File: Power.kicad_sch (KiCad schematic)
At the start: 23 parts, among them U1 21700_DUAL_HOLDER, U2 TPS63070RNMR, U3 TPRT9013-33

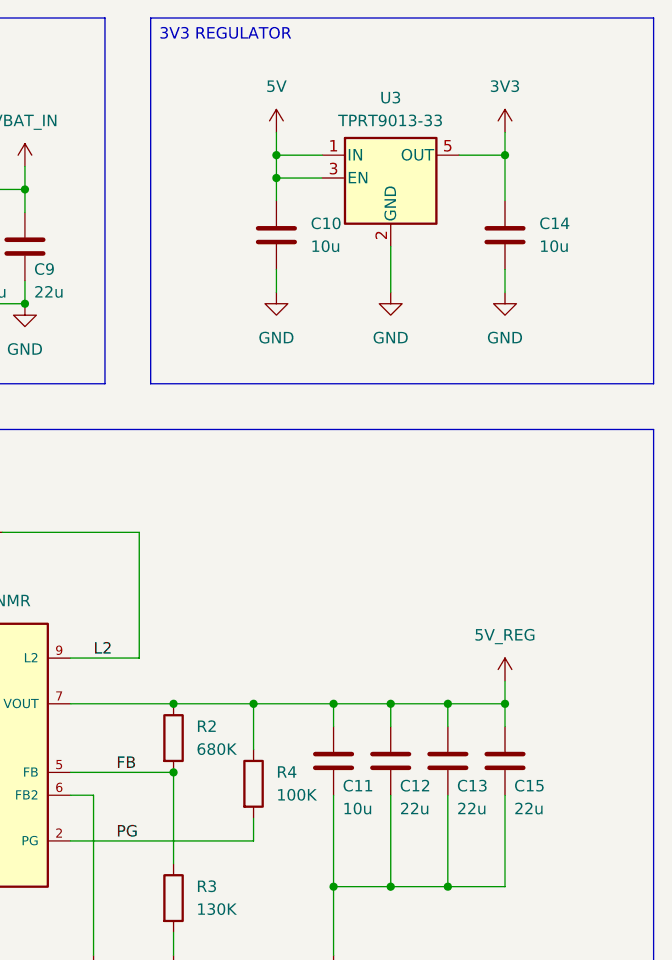
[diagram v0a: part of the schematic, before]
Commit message: Net nodes
Added the missing net nodes in the schematic.
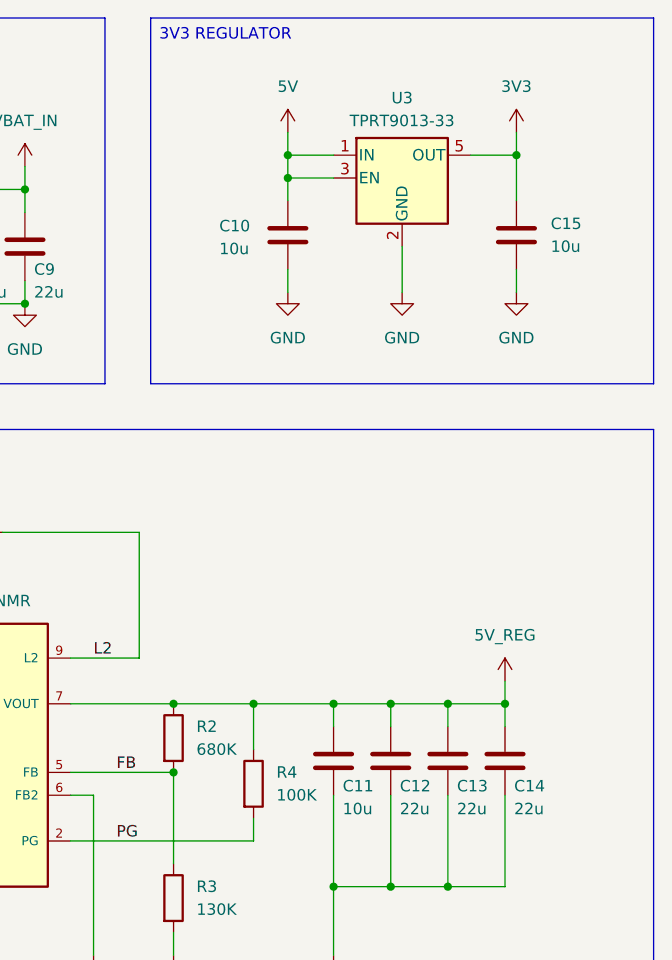
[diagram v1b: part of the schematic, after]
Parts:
- renumbered C15 to C14, C14 to C15
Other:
- moved on the sheet: C10, C15, U3

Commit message: ESC layout and footprints
Added the initial ESC layout.
Updated some footprints for compatibility.
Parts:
- C11, C3: footprint Capacitor_SMD:C_0805_2012Metric -> Capacitor_SMD:C_0603_1608Metric
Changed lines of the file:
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@@
 			)
 		)
-		(property "Footprint" "Capacitor_SMD:C_0805_2012Metric"
+		(property "Footprint" "Capacitor_SMD:C_0603_1608Metric"
 			(at 176.2252 120.65 0)
 			(effects
@@
 			)
 		)
-		(property "Footprint" "Capacitor_SMD:C_0805_2012Metric"
+		(property "Footprint" "Capacitor_SMD:C_0603_1608Metric"
 			(at 98.0948 120.65 0)
 			(effects

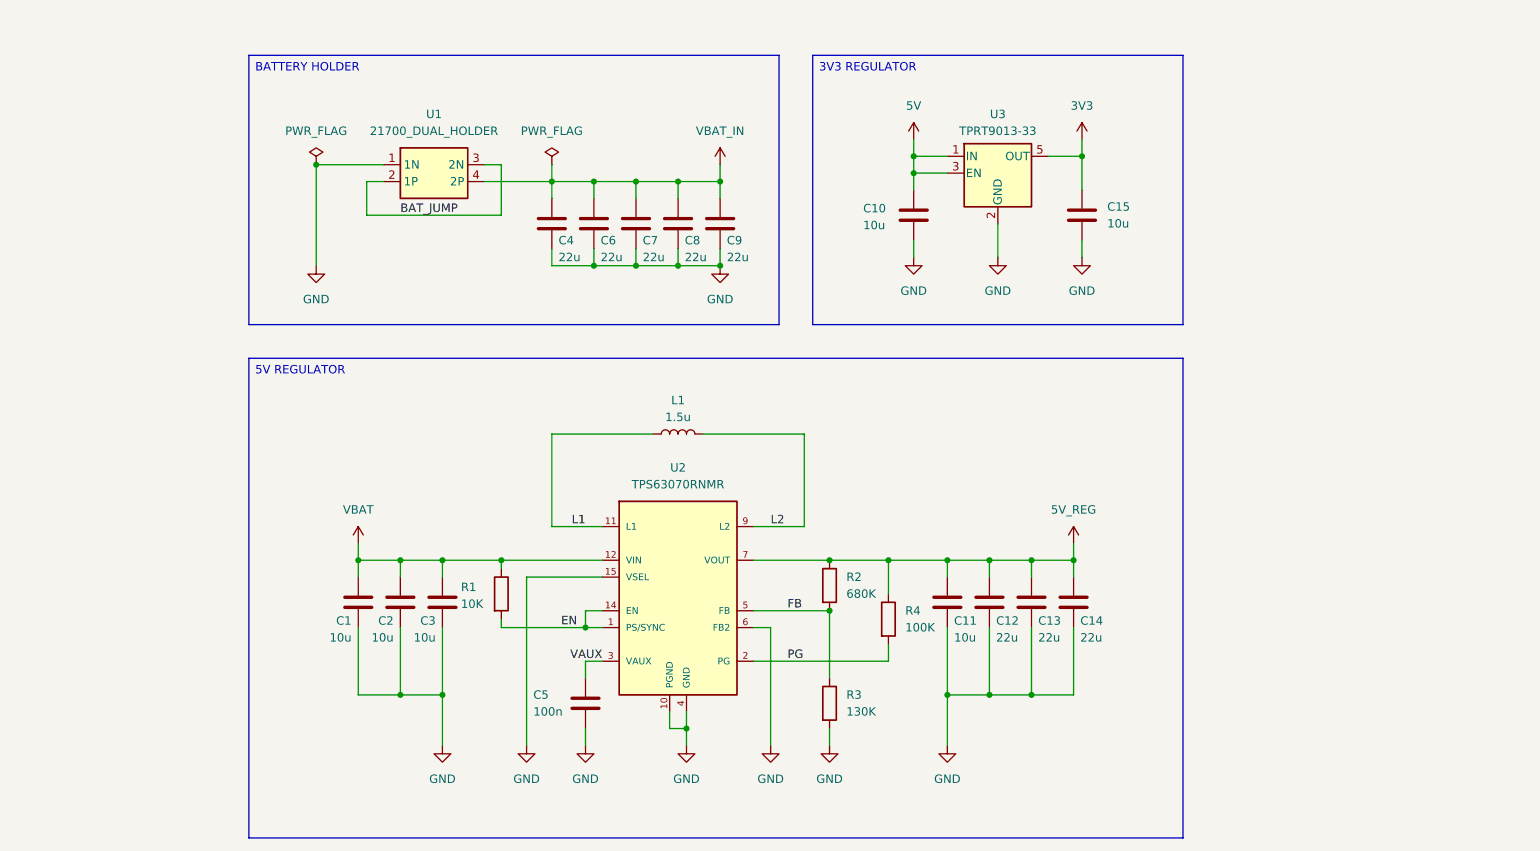
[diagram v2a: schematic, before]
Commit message: Initial layout
Completed an initial layout of the main components.

TODO
Route the ESCs and check the result.
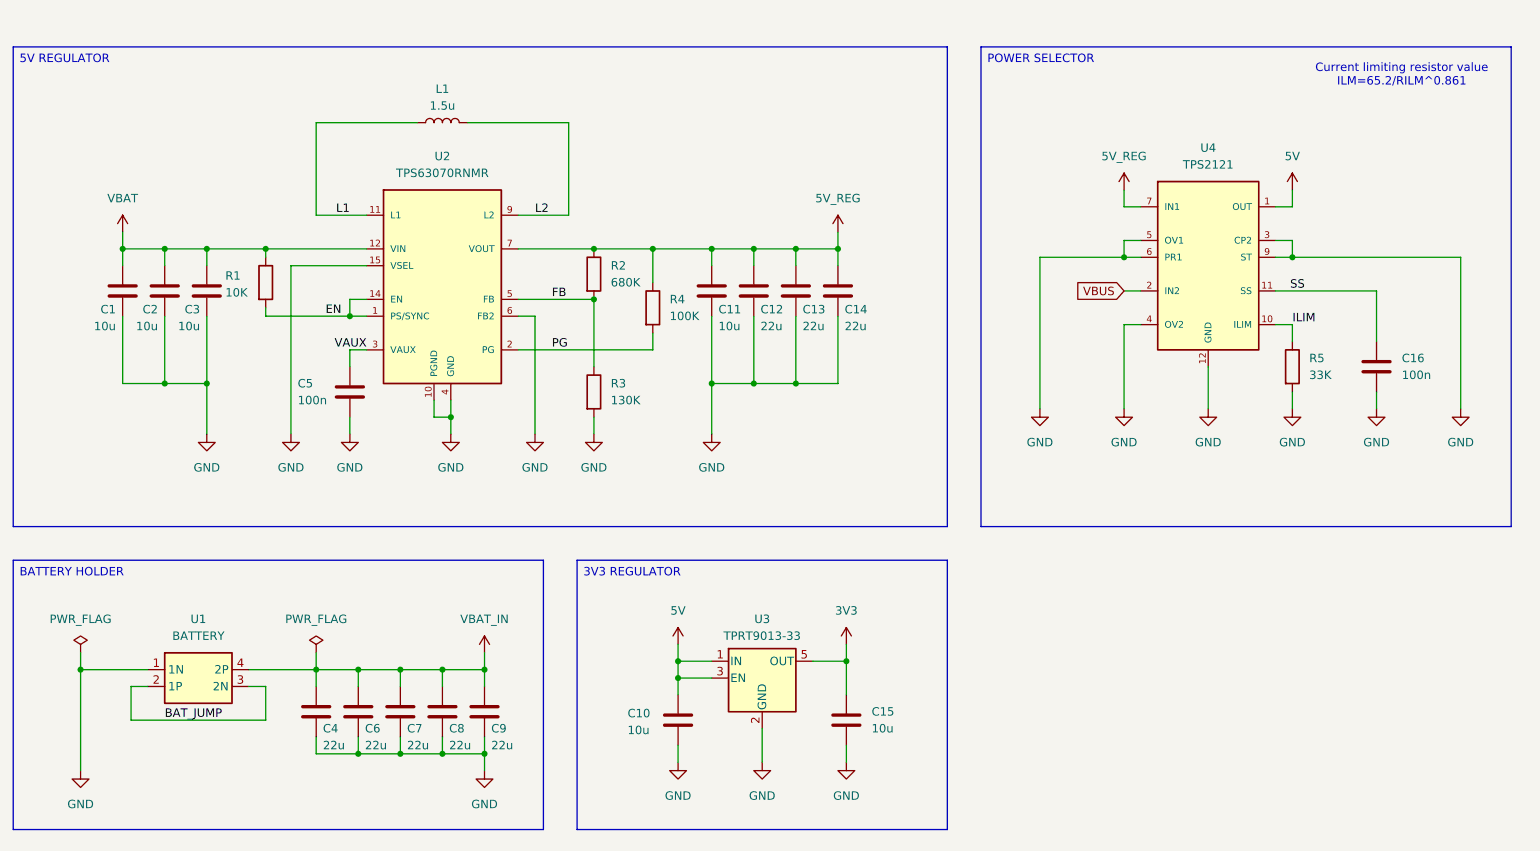
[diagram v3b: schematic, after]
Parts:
- added C16: 100n, Capacitor_SMD:C_0603_1608Metric, symbol Device:C
- added R5: 33K, Resistor_SMD:R_0603_1608Metric, symbol Device:R
- added U4: TPS2121, Custom_Parts:VQFN-HR-12_2x2.5mm_P0.5mm, symbol Custom_Parts:TPS2121
- U1: value 21700_DUAL_HOLDER -> BATTERY
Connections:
- net 5V: now also U4.1 (OUT), U4.8 (OUT)
- net 5V_REG: now also U4.7 (IN1)
- net GND: now also C16.2, R5.2, U4.12 (GND), U4.3 (CP2), U4.4 (OV2), U4.5 (OV1), U4.6 (PR1), U4.9 (ST)
- new net ILIM: R5.1, U4.10 (ILIM)
- new net SS: C16.1, U4.11 (SS)
- new net VBUS: U4.2 (IN2)
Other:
- note added: "Current limiting resistor value ILM=65.2/RILM^0.861"
- moved on the sheet: C1, C10, C11, C12, C13, C14, C15, C2, C3, C4, C5, C6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

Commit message: MCU layout
Started the MCU layout.

TODO:
Check the previous iterations.
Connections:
- net 5V_REG: now also U4.2 (IN2); no longer U4.7 (IN1)
- net VBUS: now also U4.7 (IN1); no longer U4.2 (IN2)

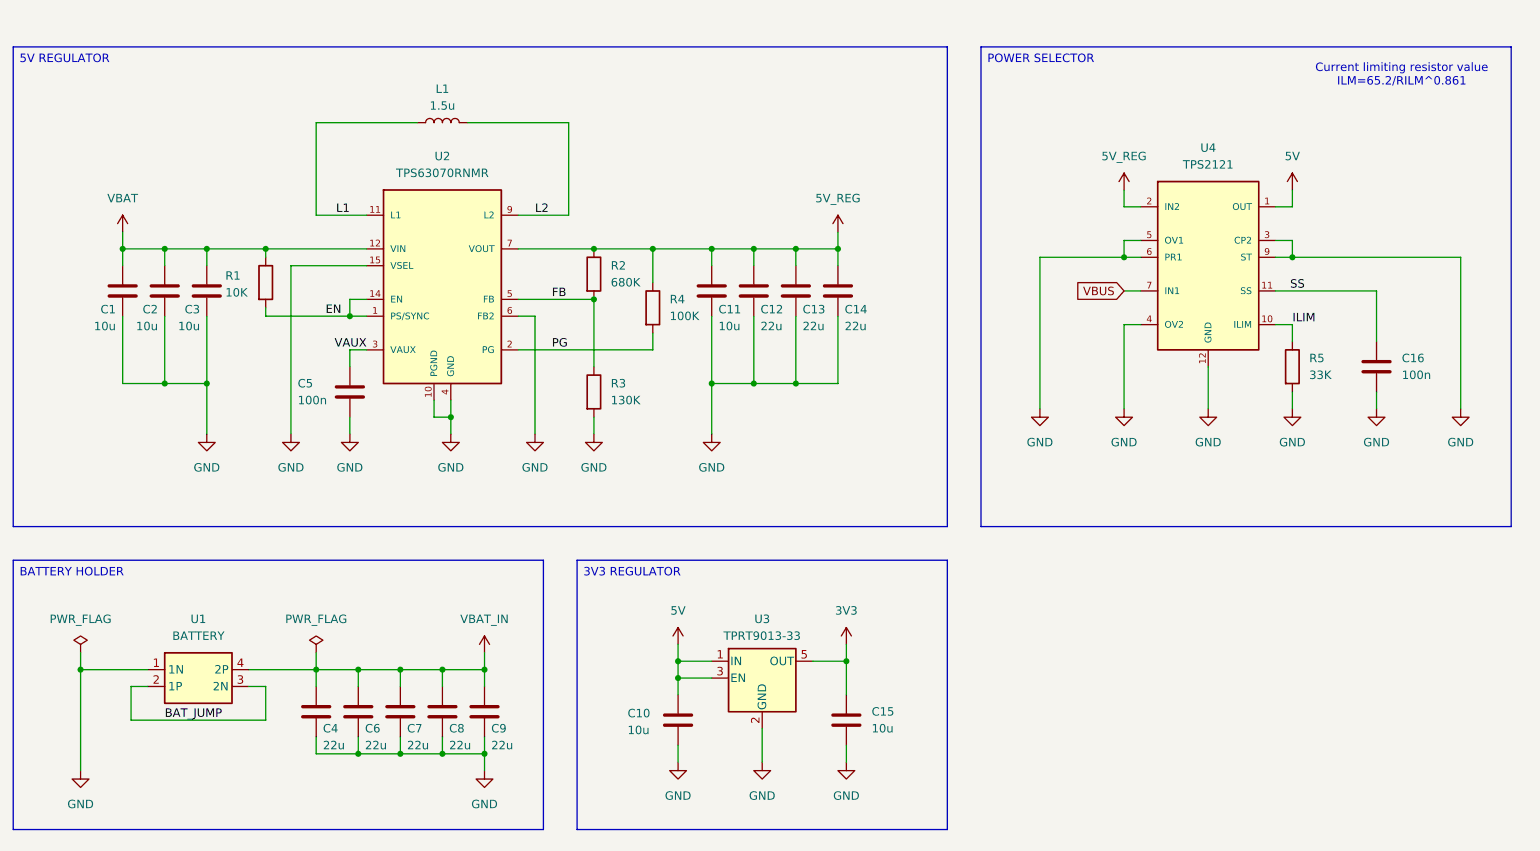
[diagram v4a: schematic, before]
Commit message: Schematic revision
Added an ESP32 C3 for the ELRS receiver.
Updated the protection approach for the board.
Updated the net nodes.
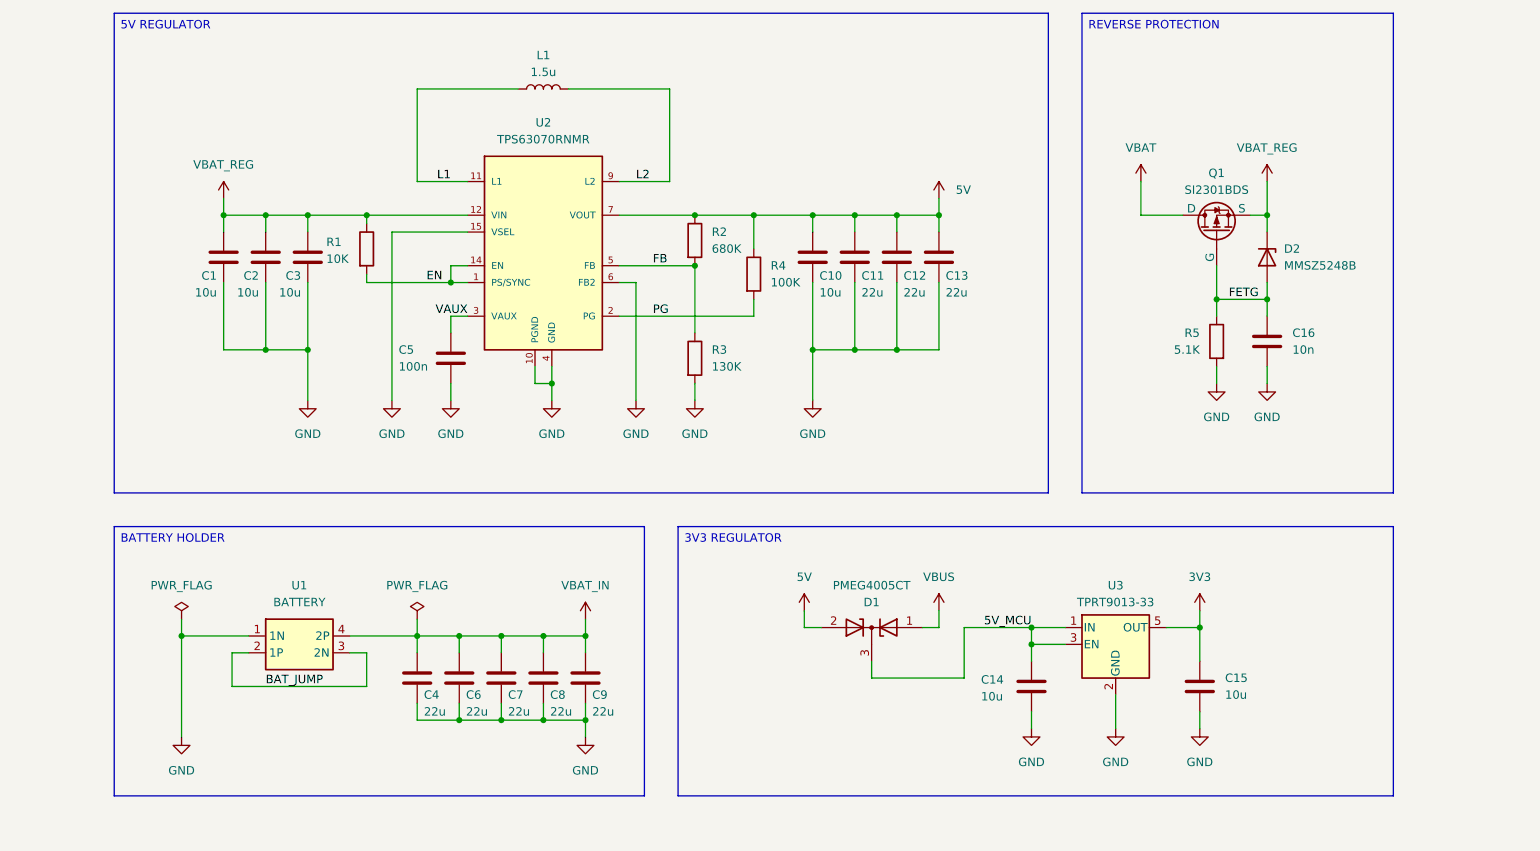
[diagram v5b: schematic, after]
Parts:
- removed U4: TPS2121, Custom_Parts:VQFN-HR-12_2x2.5mm_P0.5mm, symbol Custom_Parts:TPS2121
- added D1: PMEG4005CT, Package_TO_SOT_SMD:SOT-23, symbol Device:D_Zener_Dual_CommonCathode_AAK
- added D2: MMSZ5248B, symbol Custom_Parts:MMSZ5248B
- added Q1: SI2301BDS, Package_TO_SOT_SMD:SOT-23, symbol Custom_Parts:SI2301BDS
- C16: value 100n -> 10n
- R5: value 33K -> 5.1K
- renumbered C11 to C10, C12 to C11, C13 to C12, C14 to C13, C10 to C14
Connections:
- net 5V_REG is gone; now on net 5V: C10.1, C11.1, C12.1, C13.1, R2.1, R4.1, U2.7 (VOUT)
- net SS is gone; now on net FETG: C16.1
- net 5V: now also D1.2 (A); no longer C14.1, U3.1 (IN), U3.3 (EN)
- net VBAT: now also Q1.3 (D); no longer C1.1, C2.1, C3.1, R1.1, U2.12 (VIN)
- net VBUS: now also D1.1 (A)
- net ILIM renamed FETG
- net FETG: now also D2.2 (A), Q1.1 (G)
- new net 5V_MCU: C14.1, D1.3 (K), U3.1 (IN), U3.3 (EN)
- new net VBAT_REG: C1.1, C2.1, C3.1, D2.1 (K), Q1.2 (S), R1.1, U2.12 (VIN)
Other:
- note removed: "Current limiting resistor value ILM=65.2/RILM^0.861"
- moved on the sheet: C1, C10, C11, C12, C13, C14, C15, C2, C3, C4, C5, C6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

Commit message: Schematic and PCB
Reviewed the schematic and deleted unused components.
Updated the PCB and also removed unused footprints.
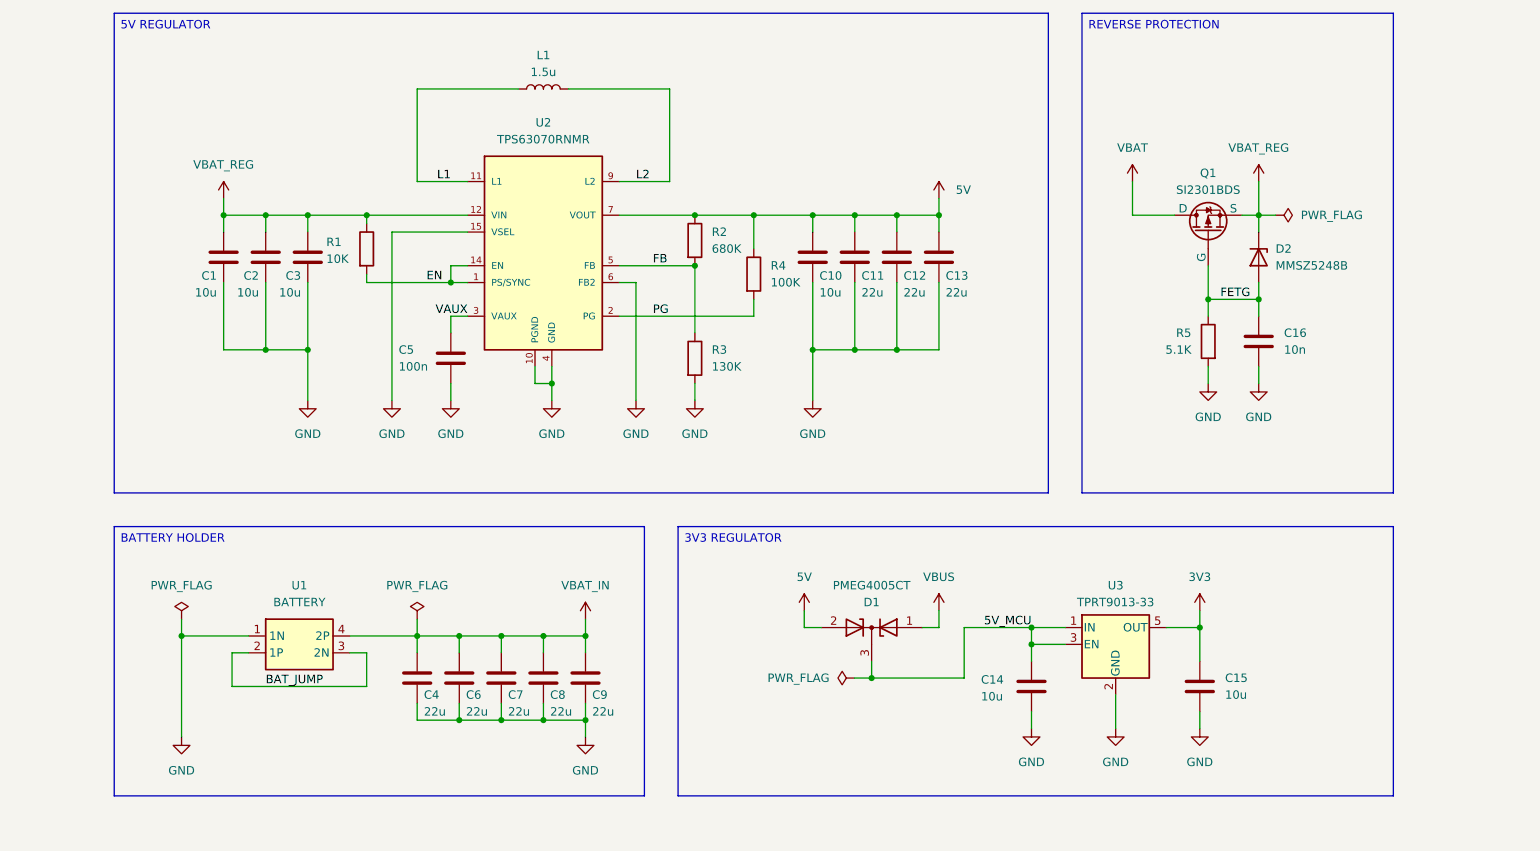
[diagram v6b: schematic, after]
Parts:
- D2: footprint (none) -> Diode_SMD:D_SOD-523
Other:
- moved on the sheet: C16, D2, Q1, R5

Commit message: IMU filtering and layout
Added a missing capacitor for the IMU.
Updated the PCB layout.
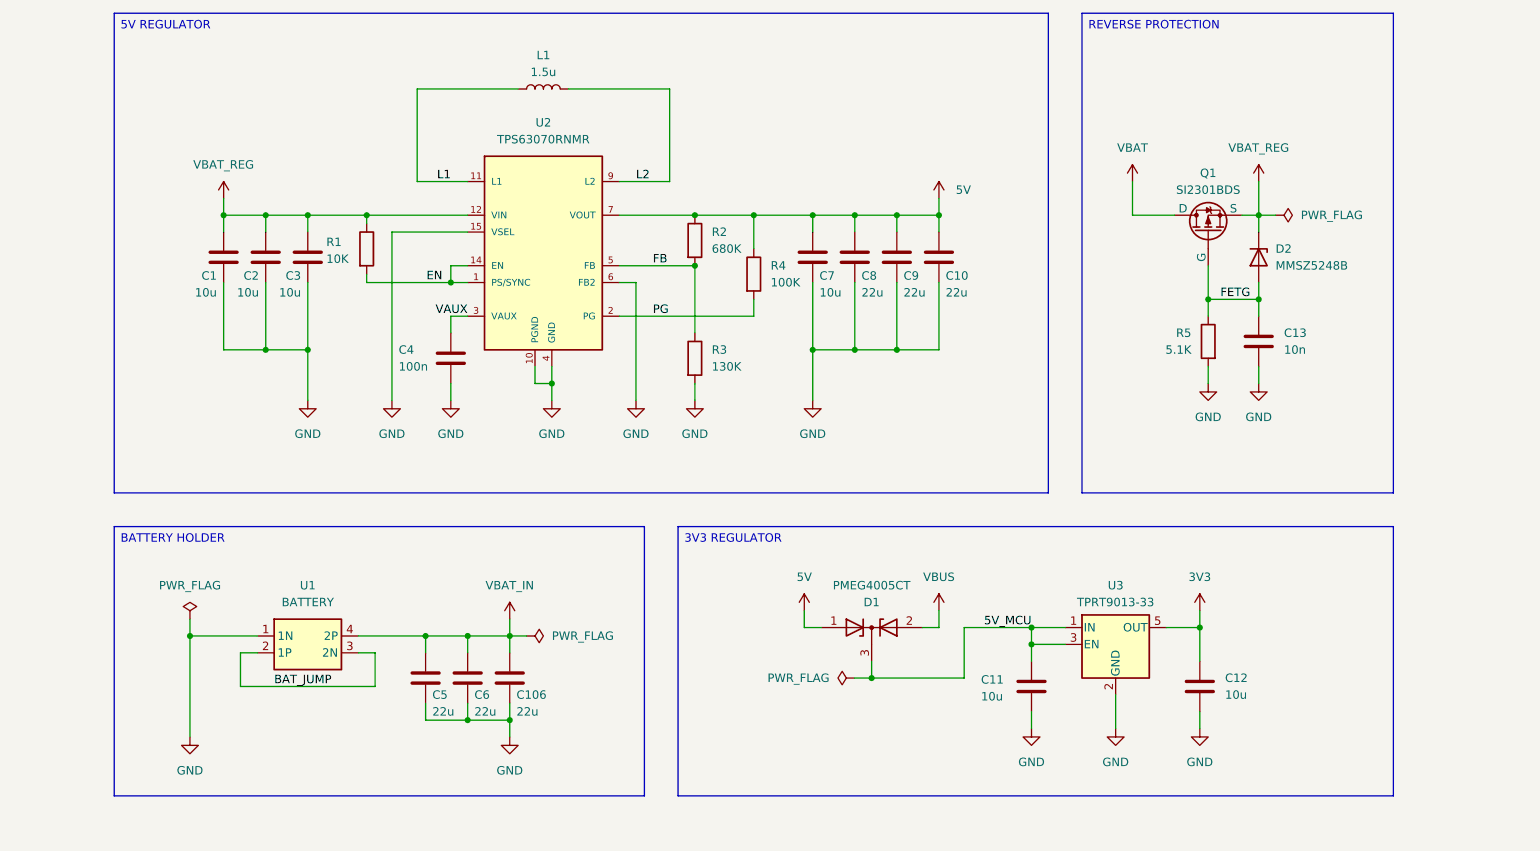
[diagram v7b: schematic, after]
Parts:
- removed C7, C8, C9: 22u, Capacitor_SMD:C_1206_3216Metric, symbol Device:C
- added C106: 22u, Capacitor_SMD:C_1206_3216Metric, symbol Device:C
- renumbered C13 to C10, C14 to C11, C15 to C12, C16 to C13, C5 to C4, C4 to C5, C10 to C7, C11 to C8, C12 to C9
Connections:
- net 5V: now also D1.1 (A); no longer D1.2 (A)
- net GND: now also C106.2
- net VBAT_IN: now also C106.1
- net VBUS: now also D1.2 (A); no longer D1.1 (A)
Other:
- moved on the sheet: C5, C6, U1
